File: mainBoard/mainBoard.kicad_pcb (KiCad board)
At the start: 4 copper layers, 274.8 x 239.2 mm, 278 parts, among them J1 1366005, J10 Conn_01x02, J11 Conn_02x05_Odd_Even, J12 Conn_01x02, J13 Conn_01x02, J14 Conn_01x06, J17 Conn_01x05, J18 Conn_01x04, J19 Conn_01x14, J2 USB_A, J3 1714971, J4 1714971, J5 4DB-P108-02, J6 4DB-P108-02, J7 4DB-P108-02, J8 Conn_01x02, J9 Conn_01x02, K1 Relay_SPDT, Q1 IRLML6244TRPBF, Q2 IRLML6244TRPBF, Q3 IRLML6244TRPBF, Q4 IRLML6244TRPBF, Q5 IRLML6244TRPBF, Q7 IRLML6244TRPBF, SW1 SW_SPST, SW2 SW_SPDT, SW3 SW_Push, SW4 SW_Push, U1 RT6255BHGJ8F, U10 DS18B20+, U11 OPA333AIDCKT, U12 OPA333AIDCKT, U13 DS18B20+, U14 DS18B20+, U15 OPA333AIDCKT, U16 DS18B20+, U17 SFH617A-2, U18 USBLC6-4SC6, U19 23LC1024-I/ST, U2 RT9059GSP, U20 LM386, U21 USBLC6-4SC6, U23 USBLC6-4SC6, U24 USBLC6-2SC6, U26 100, U27 100, U28 100, U29 100, U3 RT9059GSP, U30 74LVC1T45W6-7, U32 74LVC1T45W6-7, U4 TPS2041B, U5 USBLC6-2SC6, U6 STM32F413RHT6, U7 MOC3083S-TA1, U8 MOC3083S-TA1, U9 DS18B20+, Y1 RH100-48.000-10-F-1015-X-TR-N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

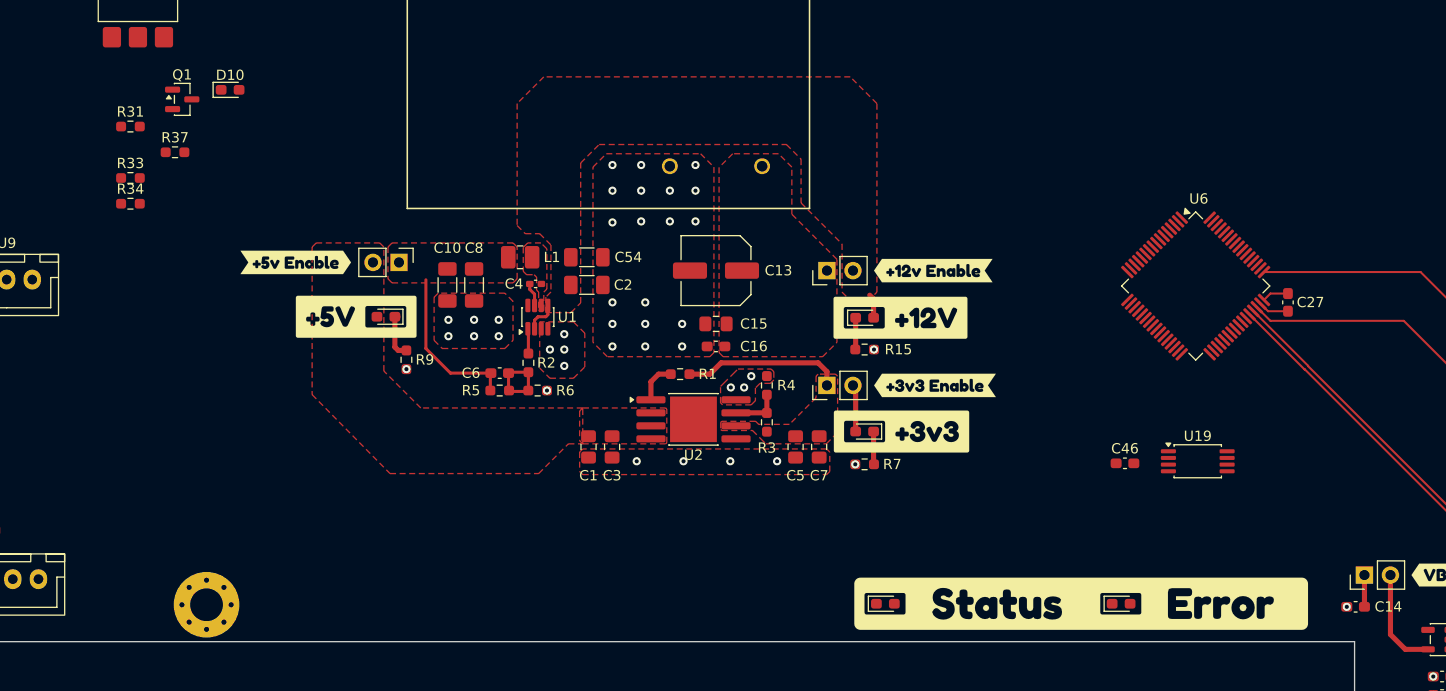
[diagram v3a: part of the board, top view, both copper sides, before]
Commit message: work on layout, change to larger inductor
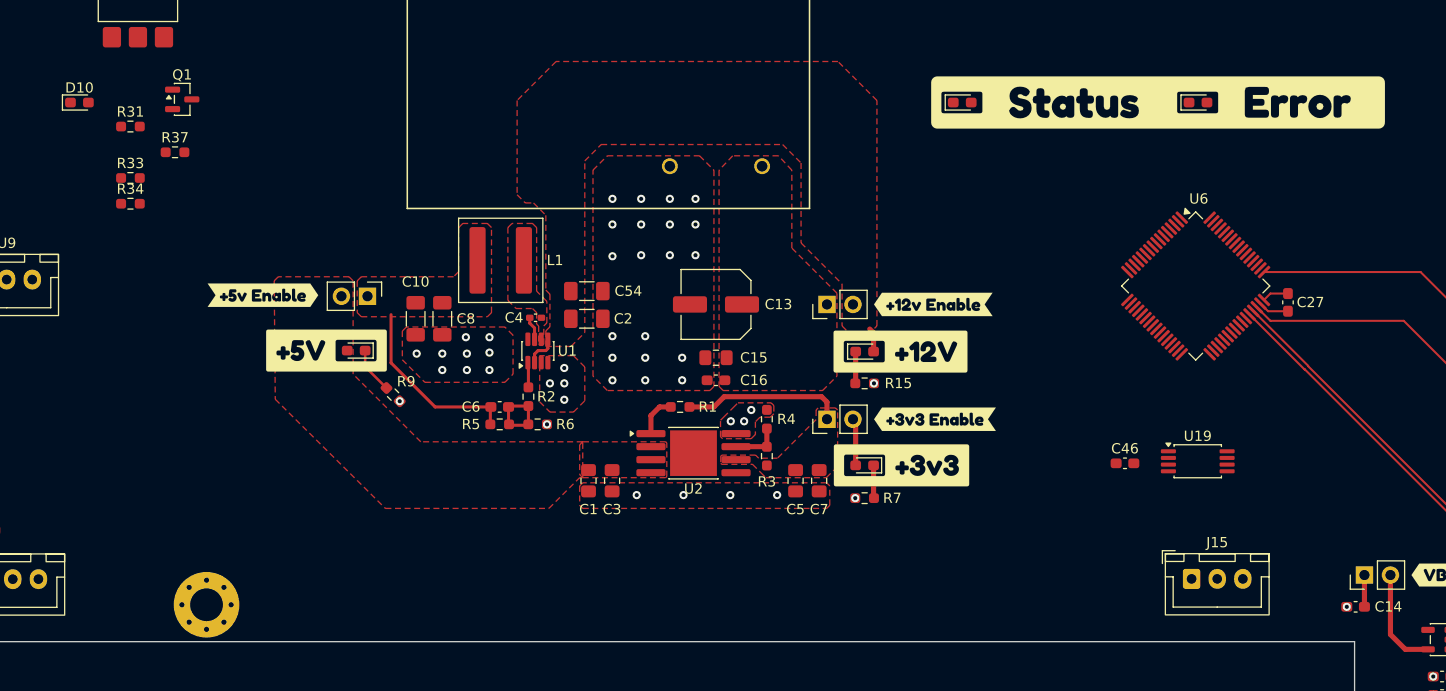
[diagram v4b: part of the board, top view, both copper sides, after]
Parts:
- added J15: Conn_01x03, Connector_JST:JST_XH_B3B-XH-A_1x03_P2.50mm_Vertical, F.Cu at (294.5, 176.5)
- L1: footprint Inductor_SMD:L_1008_2520Metric_Pad1.43x2.20mm_HandSolder -> Inductor_SMD:L_Coilcraft_XAL7030-472
- moved D6 49.5 mm to (272.1, 130.0)
- moved D7 49.5 mm to (295.1, 130.0)
- moved kobee-studio-6A78A548 49.5 mm to (291.2, 130.0)
- moved D10 14.8 mm to (186.0, 130.0)
- moved C10 4.53 mm to (218.8, 151.1)
- moved C8 4.53 mm to (221.4, 151.1)
- moved kobee-studio-6A78B9B1 4.53 mm to (203.9, 148.8)
- moved JP2 4.51 mm to (214.1, 148.9)
- moved D2 4.39 mm to (213.0, 154.2)
- moved kobee-studio-6A78B988 4.39 mm to (210.1, 154.2)
- moved R9 3.64 mm to (216.6, 158.5), turned to -45 degrees
- moved C1 3.30 mm to (235.7, 166.9)
- moved C15 3.30 mm to (248.1, 154.9)
- moved C3 3.30 mm to (238.0, 166.9)
- moved C4 3.30 mm to (230.5, 151.0)
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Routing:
- net Net-(JP2-A): track 15.8 -> 17.9 mm
- net GND: vias 67 -> 71

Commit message: add to layout
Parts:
- added kobee-studio-6A7A4227: Kobee Studio, kobee-studio-6A7A4227, F.Cu at (307.9, 89.9)
- added kobee-studio-6A7A4332: Kobee Studio, kobee-studio-6A7A42ED, F.Cu at (285.3, 98.3)
- moved REF** 139.0 mm to (278.1, 124.2)
- moved R78 22.6 mm to (297.3, 97.1), turned to 180 degrees
- moved R74 18.9 mm to (297.3, 108.9)
- moved D17 16.8 mm to (315.1, 108.9), turned to 180 degrees
- moved U17 7.45 mm to (311.7, 108.9), turned to 180 degrees
- moved D6 1.83 mm to (273.9, 129.9)
- moved D7 1.83 mm to (296.9, 129.9)
- moved kobee-studio-6A78A548 1.83 mm to (293.1, 129.9)
- moved J12 0.36 mm to (310.4, 97.1)
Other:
- board text added: "Michael Pate Version 3.3 08/2026"
- board text removed: "Michael Pate Version 3.1 06/2026"

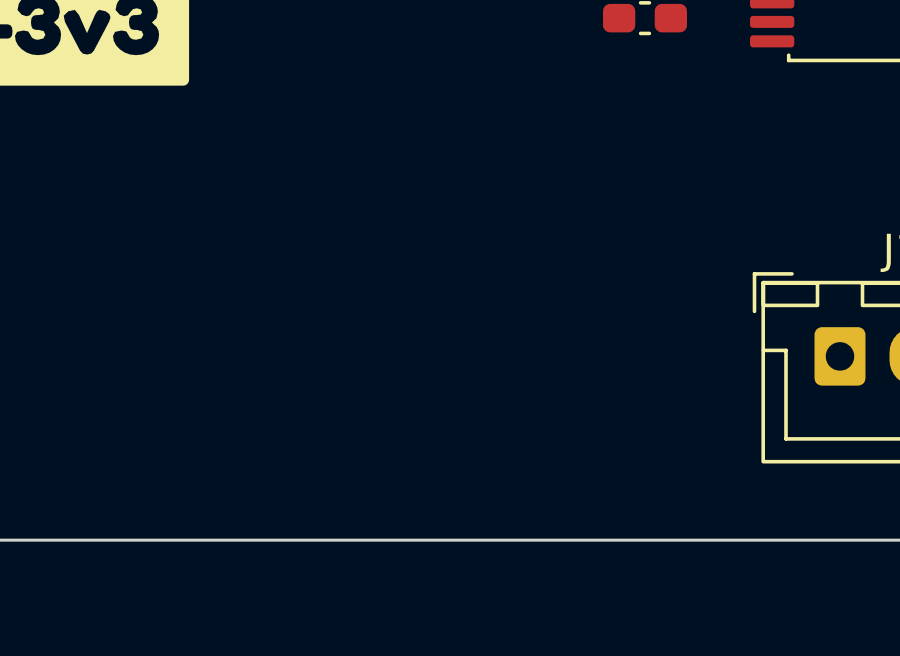
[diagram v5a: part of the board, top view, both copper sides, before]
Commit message: add NOR flash for UI
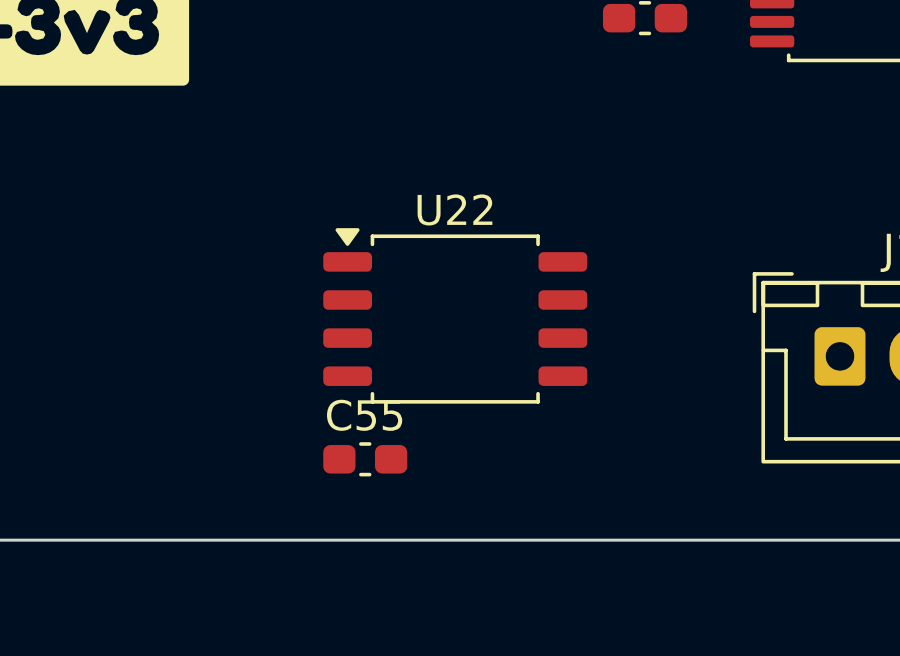
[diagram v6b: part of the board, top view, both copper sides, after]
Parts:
- added C55: 100nF, Capacitor_SMD:C_0603_1608Metric_Pad1.08x0.95mm_HandSolder, F.Cu at (278.7, 179.9)
- added U22: W25Q64JVSSIM TR, Package_SO:SOIC-8_5.3x5.3mm_P1.27mm, F.Cu at (281.7, 175.2)
